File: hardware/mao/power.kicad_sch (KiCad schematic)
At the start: 33 parts, among them J101 USB-C, J102 BAT, Q101 AO3401A, U101 TPD2E2U06, U102 BQ25185DLHR, U103 MAX17048G+T10, U104 TPS62840DLCR, U105 TPS22916CYFPR

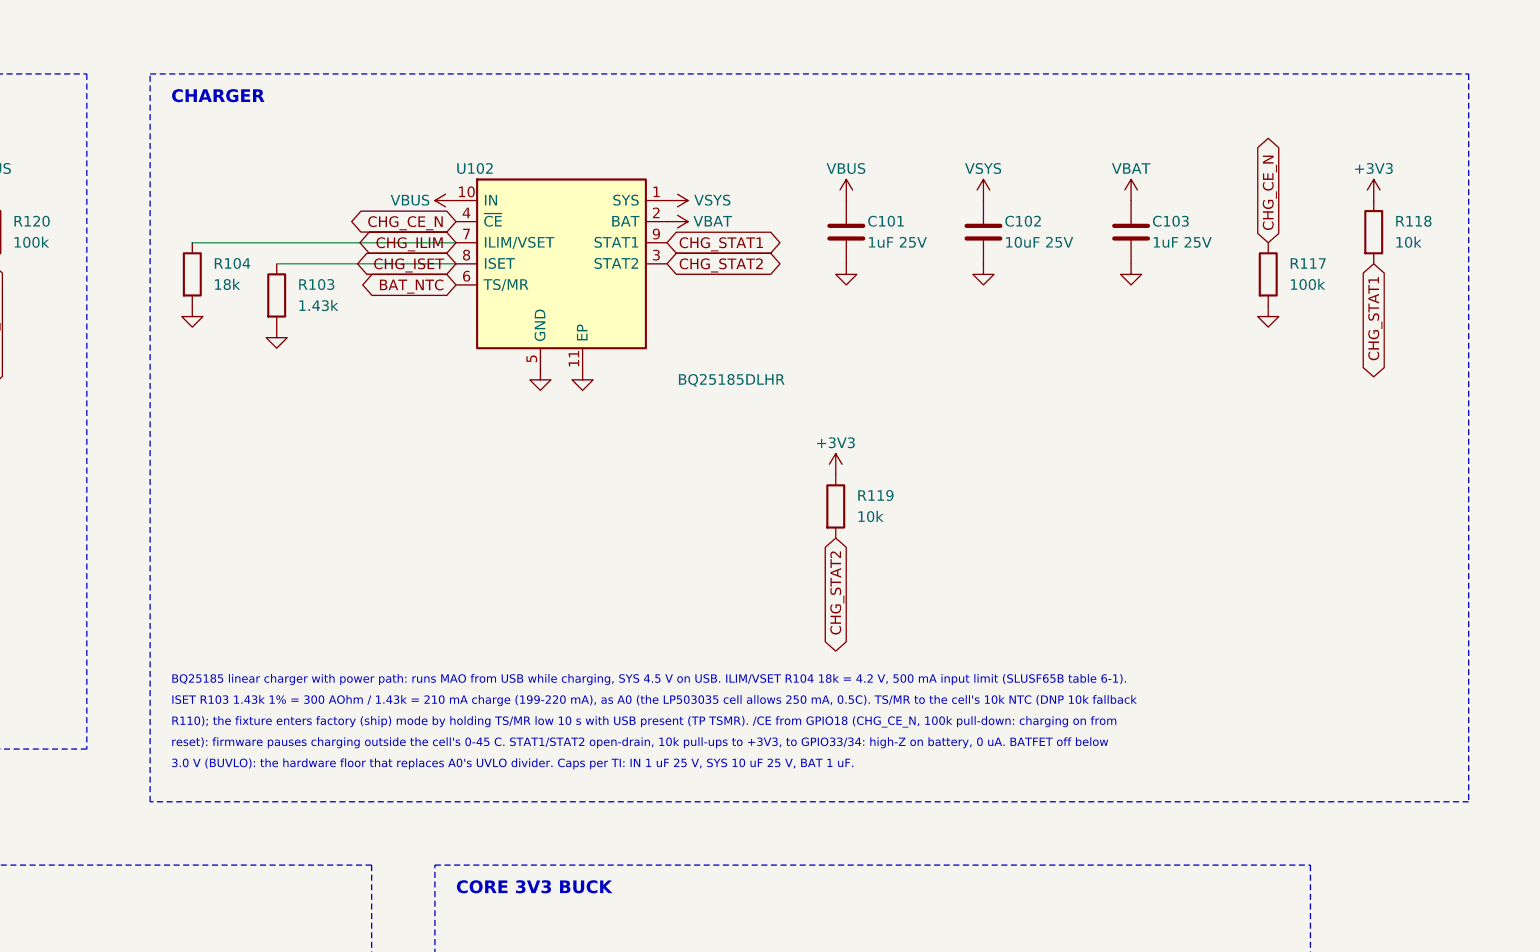
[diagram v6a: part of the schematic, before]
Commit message: A1 BOM (design review 2026-10-06): charger IN/BAT 2.2 uF 25 V 0402, DRV2605LDGST, DMG2302UKQ-7; backlight reference 95.8 mV -> 29.0 mA
C101/C103 move from 1 uF to 2.2 uF 25 V 0402 (CL05A225KA5NUNC, C307418) so at least 1 uF remains under DC bias
(TI SLUSF65B 7.2.2.3). DRV2605LDGSR -> DRV2605LDGST (C425927, same part, 250 reel) and DMG2302UK-7 -> DMG2302UKQ-7
(C5224573, same pinout) for stock. Fixes the backlight arithmetic in the capture notes (N7).

Co-Authored-By: Claude Opus 5.5 <noreply@anthropic.com>
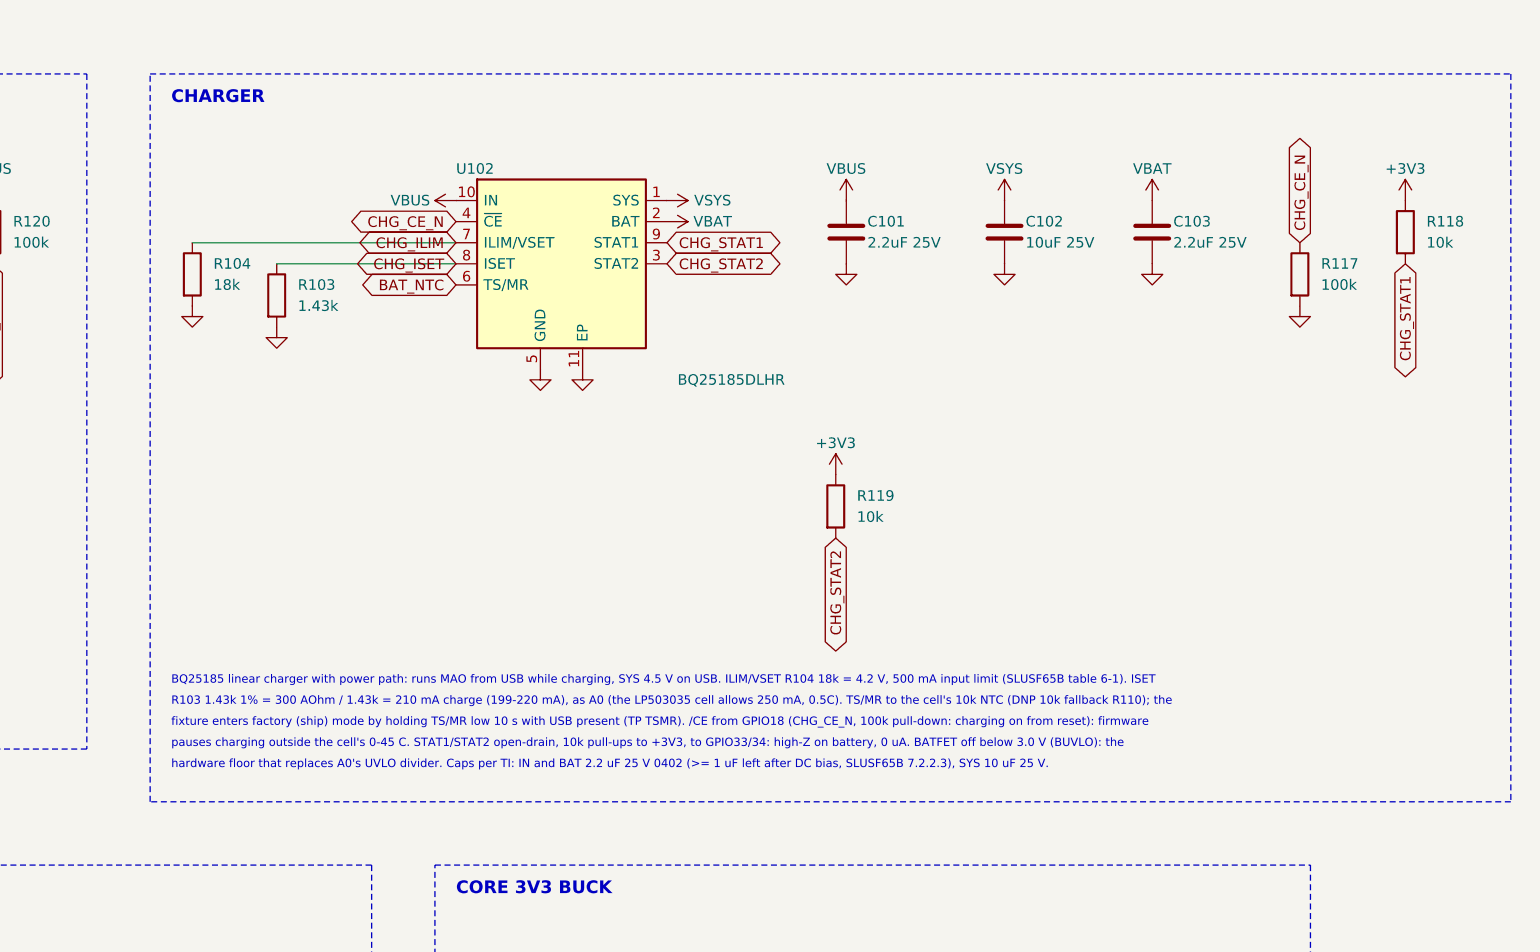
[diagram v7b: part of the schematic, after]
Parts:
- C101, C103: value 1uF 25V -> 2.2uF 25V; LCSC C52923 -> C307418; MPN CL05A105KA5NQNC -> CL05A225KA5NUNC
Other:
- note added: "BQ25185 linear charger with power path: runs MAO from USB while charging, SYS 4.5 V on USB. ILIM/VSET R104 18k = 4.2 V, 500 mA input limit (SLUSF65B table 6-1). ISET"
- note added: "R103 1.43k 1% = 300 AOhm / 1.43k = 210 mA charge (199-220 mA), as A0 (the LP503035 cell allows 250 mA, 0.5C). TS/MR to the cell's 10k NTC (DNP 10k fallback R110); the"
- note added: "fixture enters factory (ship) mode by holding TS/MR low 10 s with USB present (TP TSMR). /CE from GPIO18 (CHG_CE_N, 100k pull-down: charging on from reset): firmware"
- note added: "hardware floor that replaces A0's UVLO divider. Caps per TI: IN and BAT 2.2 uF 25 V 0402 (>= 1 uF left after DC bias, SLUSF65B 7.2.2.3), SYS 10 uF 25 V."
- note added: "pauses charging outside the cell's 0-45 C. STAT1/STAT2 open-drain, 10k pull-ups to +3V3, to GPIO33/34: high-Z on battery, 0 uA. BATFET off below 3.0 V (BUVLO): the"
- note removed: "3.0 V (BUVLO): the hardware floor that replaces A0's UVLO divider. Caps per TI: IN 1 uF 25 V, SYS 10 uF 25 V, BAT 1 uF."
- note removed: "BQ25185 linear charger with power path: runs MAO from USB while charging, SYS 4.5 V on USB. ILIM/VSET R104 18k = 4.2 V, 500 mA input limit (SLUSF65B table 6-1)."
- note removed: "ISET R103 1.43k 1% = 300 AOhm / 1.43k = 210 mA charge (199-220 mA), as A0 (the LP503035 cell allows 250 mA, 0.5C). TS/MR to the cell's 10k NTC (DNP 10k fallback"
- note removed: "R110); the fixture enters factory (ship) mode by holding TS/MR low 10 s with USB present (TP TSMR). /CE from GPIO18 (CHG_CE_N, 100k pull-down: charging on from"
- note removed: "reset): firmware pauses charging outside the cell's 0-45 C. STAT1/STAT2 open-drain, 10k pull-ups to +3V3, to GPIO33/34: high-Z on battery, 0 uA. BATFET off below"
- moved on the sheet: C102, C103, R117, R118

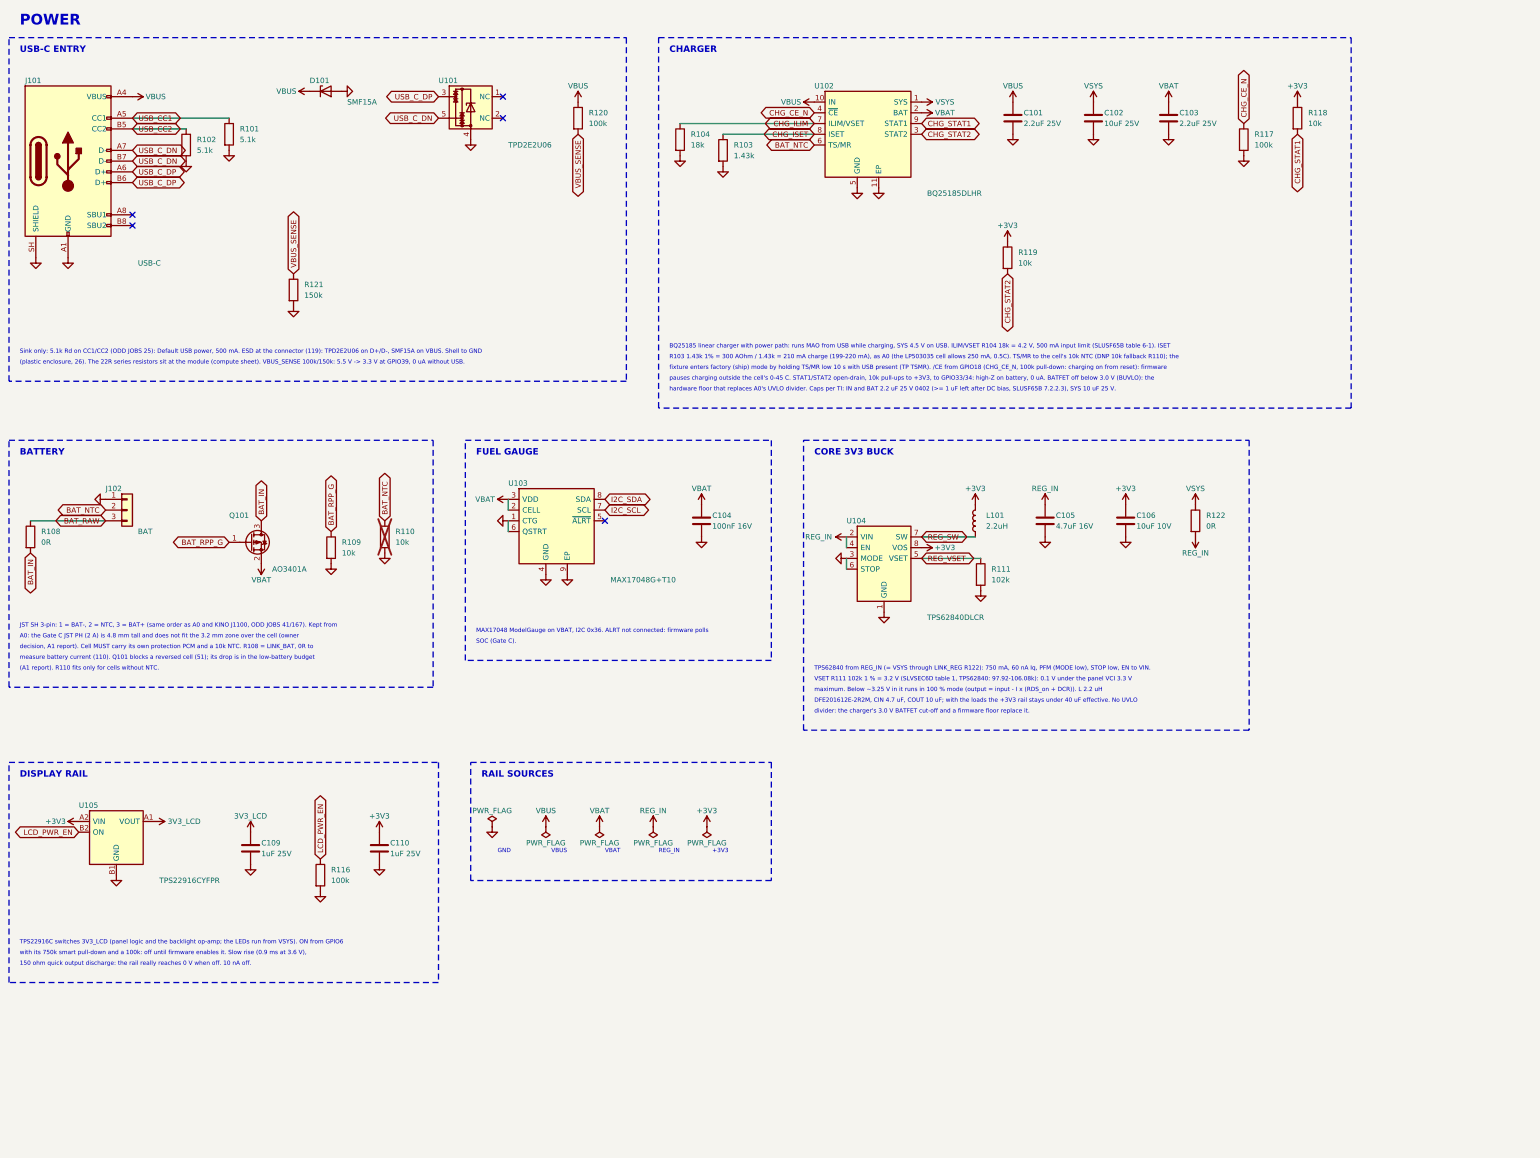
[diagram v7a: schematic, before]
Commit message: A1: USB wakes from deep sleep (design review 2026-10-06, finding 1)
VBUS_SENSE (GPIO39) is not an RTC pad. The 100k/150k VBUS divider now drives a 2N7002 (Q102, C8545 Basic) whose
drain, USB_PRESENT_N (100k pull-up R123, 33 uA only while USB is present), sits on the spare RTC pad GPIO2: an ext1
any-low wake source. GPIO39 is a spare with test pad TP26; TP24 now probes USB_PRESENT_N.

Layout (surgical, route_review.py): Q102/R123 on F east of the module's right escape column, gate on the router's
VBUS_SENSE line, drain down to an L3 run under the module (south of AMP_LRCLK) to GPIO2's stub; sync_fields.py --add
puts parts new in circuit.py on the routed board. DRC 0 / unconnected 0 / parity 0, planes continuous.

Firmware: MAO_LINE_USB_PRESENT reads GPIO2 active low, USB_PRESENT_N joins the A1 ext1 any-low mask when it idles
high (deep_sleep_hold and the critical sleep ask for it); MAO still never deep-sleeps with USB present.

Co-Authored-By: Claude Opus 5.5 <noreply@anthropic.com>
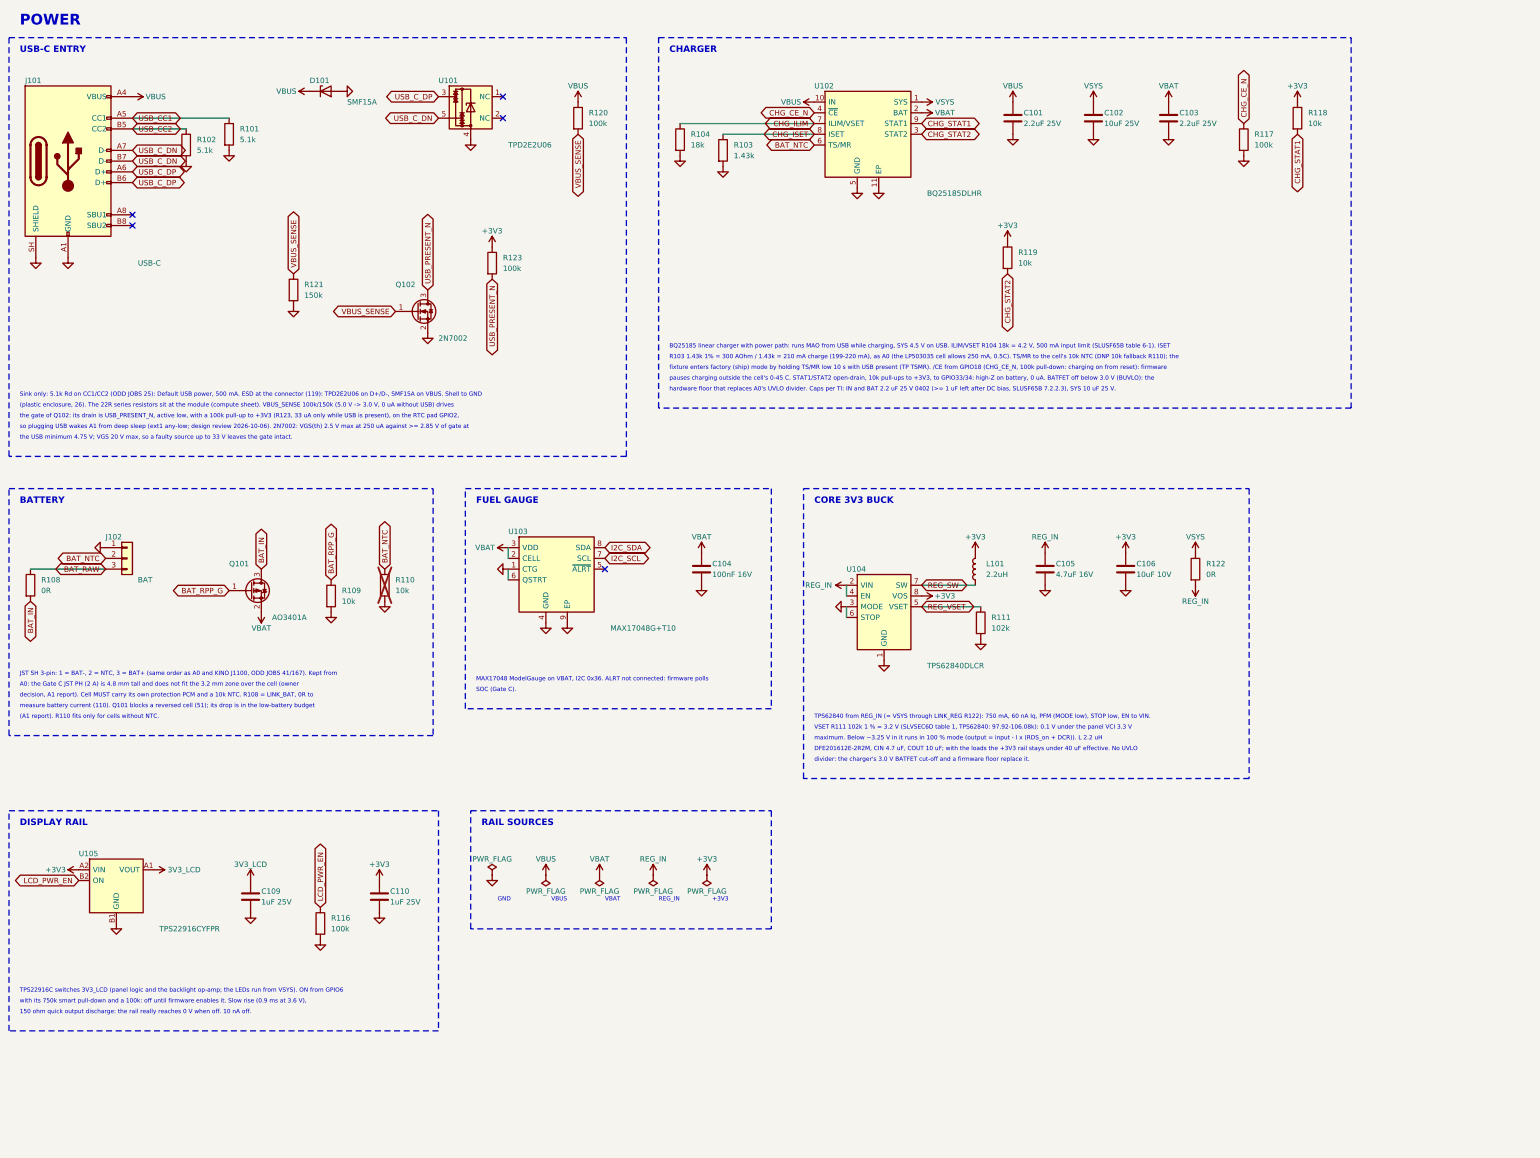
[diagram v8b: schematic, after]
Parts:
- added Q102: 2N7002, Package_TO_SOT_SMD:SOT-23, symbol Transistor_FET:2N7002
- added R123: 100k, Resistor_SMD:R_0402_1005Metric, symbol Device:R
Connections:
- net +3V3: now also R123.1
- net GND: now also Q102.2 (S)
- net VBUS_SENSE: now also Q102.1 (G)
- new net USB_PRESENT_N: Q102.3 (D), R123.2
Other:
- note added: "(plastic enclosure, 26). The 22R series resistors sit at the module (compute sheet). VBUS_SENSE 100k/150k (5.0 V -> 3.0 V, 0 uA without USB) drives"
- note added: "so plugging USB wakes A1 from deep sleep (ext1 any-low; design review 2026-10-06). 2N7002: VGS(th) 2.5 V max at 250 uA against >= 2.85 V of gate at"
- note added: "the USB minimum 4.75 V; VGS 20 V max, so a faulty source up to 33 V leaves the gate intact."
- note added: "the gate of Q102: its drain is USB_PRESENT_N, active low, with a 100k pull-up to +3V3 (R123, 33 uA only while USB is present), on the RTC pad GPIO2,"
- note removed: "(plastic enclosure, 26). The 22R series resistors sit at the module (compute sheet). VBUS_SENSE 100k/150k: 5.5 V -> 3.3 V at GPIO39, 0 uA without USB."
- moved on the sheet: C104, C105, C106, C109, C110, J102, L101, Q101, R108, R109, R110, R111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
